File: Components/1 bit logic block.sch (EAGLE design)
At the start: 2 parts

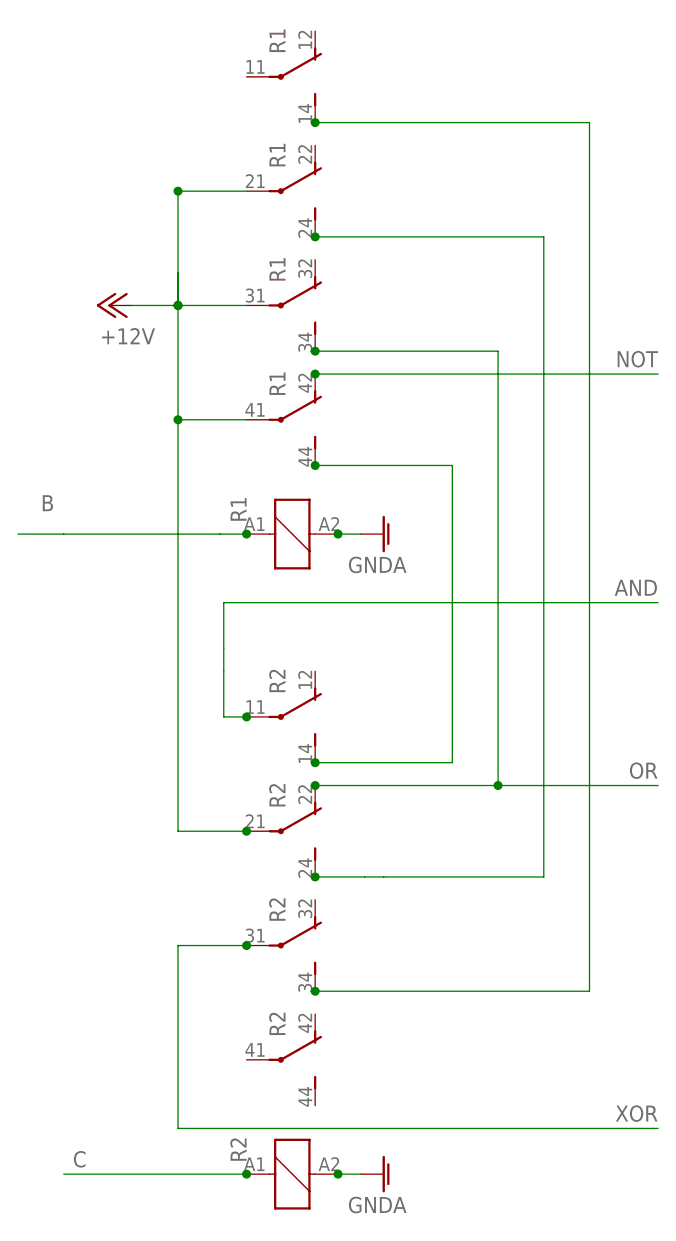
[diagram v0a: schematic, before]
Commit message: Fixed wiring for 1 bit logic block
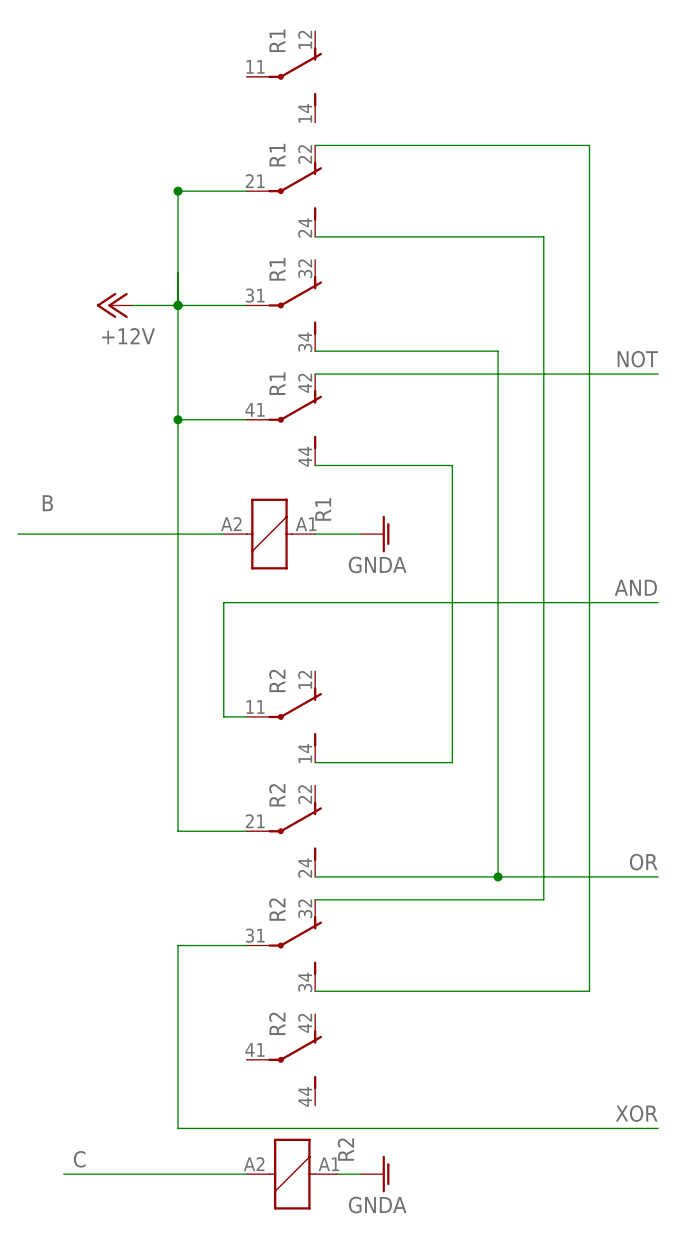
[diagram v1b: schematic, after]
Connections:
- net B: now also R11.2; no longer R11.1
- net C: now also R21.2; no longer R21.1
- net GNDA: now also R11.1, R21.1; no longer R11.2, R21.2
- net N$1: now also R24.O; no longer R23.S
- net N$3: now also R13.O; no longer R12.S
- net OR: now also R23.S; no longer R23.O
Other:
- moved on the sheet: R1
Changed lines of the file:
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@@
 <?xml version="1.0" encoding="utf-8"?>
 <!DOCTYPE eagle SYSTEM "eagle.dtd">
-<eagle version="8.1.0">
+<eagle version="8.2.1">
 <drawing>
 <settings>
@@
 <instance part="GND1" gate="1" x="96.52" y="91.44" rot="R90"/>
 <instance part="P+1" gate="1" x="66.04" y="116.84" rot="R90"/>
-<instance part="R1" gate="1" x="86.36" y="91.44" rot="R90"/>
+<instance part="R1" gate="1" x="83.82" y="91.44" rot="MR90"/>
 <instance part="R1" gate="2" x="83.82" y="142.24" rot="MR90"/>
 <instance part="R1" gate="3" x="83.82" y="129.54" rot="MR90"/>
 <instance part="R1" gate="4" x="83.82" y="116.84" rot="MR90"/>
 <instance part="R1" gate="5" x="83.82" y="104.14" rot="MR90"/>
-<instance part="R2" gate="1" x="86.36" y="20.32" rot="R90"/>
+<instance part="R2" gate="1" x="86.36" y="20.32" rot="MR90"/>
 <instance part="R2" gate="2" x="83.82" y="71.12" rot="MR90"/>
 <instance part="R2" gate="3" x="83.82" y="58.42" rot="MR90"/>
@@
 <net name="GNDA" class="0">
 <segment>
+<pinref part="GND2" gate="1" pin="GNDA"/>
+<wire x1="93.98" y1="20.32" x2="91.44" y2="20.32" width="0.1524" layer="91"/>
+<pinref part="R2" gate="1" pin="1"/>
+</segment>
+<segment>
+<pinref part="R1" gate="1" pin="1"/>
+<wire x1="88.9" y1="91.44" x2="93.98" y2="91.44" width="0.1524" layer="91"/>
+<pinref part="GND1" gate="1" pin="GNDA"/>
+</segment>
+</net>
+<net name="B" class="0">
+<segment>
+<label x="58.42" y="93.98" size="1.778" layer="95"/>
+<wire x1="55.88" y1="91.44" x2="78.74" y2="91.44" width="0.1524" layer="91"/>
 <pinref part="R1" gate="1" pin="2"/>
-<junction x="91.44" y="91.44"/>
-<pinref part="GND1" gate="1" pin="GNDA"/>
-<wire x1="91.44" y1="91.44" x2="93.98" y2="91.44" width="0.1524" layer="91"/>
-</segment>
-<segment>
-<pinref part="GND2" gate="1" pin="GNDA"/>
+</segment>
+</net>
+<net name="C" class="0">
+<segment>
+<label x="63.5" y="22.86" size="1.778" layer="95" rot="R180"/>
+<wire x1="60.96" y1="20.32" x2="81.28" y2="20.32" width="0.1524" layer="91"/>
 <pinref part="R2" gate="1" pin="2"/>
-<wire x1="93.98" y1="20.32" x2="91.44" y2="20.32" width="0.1524" layer="91"/>
-<junction x="91.44" y="20.32"/>
-</segment>
-</net>
-<net name="B" class="0">
-<segment>
-<wire x1="55.88" y1="91.44" x2="60.96" y2="91.44" width="0.1524" layer="91"/>
-<label x="58.42" y="93.98" size="1.778" layer="95"/>
-<pinref part="R1" gate="1" pin="1"/>
-<wire x1="60.96" y1="91.44" x2="78.327596875" y2="91.44" width="0.1524" layer="91"/>
-<wire x1="81.28" y1="91.44" x2="78.327596875" y2="91.44" width="0.1524" layer="91"/>
-<junction x="81.28" y="91.44"/>
-</segment>
-</net>
-<net name="C" class="0">
-<segment>
-<label x="63.5" y="22.86" size="1.778" layer="95" rot="R180"/>
-<pinref part="R2" gate="1" pin="1"/>
-<wire x1="60.96" y1="20.32" x2="81.28" y2="20.32" width="0.1524" layer="91"/>
-<junction x="81.28" y="20.32"/>
 </segment>
 </net>
@@
 <junction x="73.66" y="104.14"/>
 <wire x1="73.66" y1="116.84" x2="73.66" y2="120.4952875" width="0.1524" layer="91"/>
-<pinref part="R1" gate="5" pin="P"/>
 <wire x1="73.66" y1="104.14" x2="81.28" y2="104.14" width="0.1524" layer="91"/>
 <junction x="73.66" y="116.84"/>
-<pinref part="R1" gate="4" pin="P"/>
 <wire x1="73.66" y1="116.84" x2="81.28" y2="116.84" width="0.1524" layer="91"/>
 <junction x="73.66" y="129.54"/>
+<wire x1="73.66" y1="129.54" x2="81.28" y2="129.54" width="0.1524" layer="91"/>
+<wire x1="81.28" y1="58.42" x2="73.66" y2="58.42" width="0.1524" layer="91"/>
+<pinref part="R1" gate="5" pin="P"/>
+<pinref part="R1" gate="4" pin="P"/>
 <pinref part="R1" gate="3" pin="P"/>
-<wire x1="73.66" y1="129.54" x2="81.28" y2="129.54" width="0.1524" layer="91"/>
 <pinref part="R2" gate="3" pin="P"/>
-<wire x1="81.28" y1="58.42" x2="73.66" y2="58.42" width="0.1524" layer="91"/>
-<junction x="81.28" y="58.42"/>
 </segment>
 </net>
@@
 <wire x1="73.66" y1="25.4" x2="127" y2="25.4" width="0.1524" layer="91"/>
 <label x="127" y="27.94" size="1.778" layer="95" rot="R180"/>
+<wire x1="81.28" y1="45.72" x2="73.66" y2="45.72" width="0.1524" layer="91"/>
 <pinref part="R2" gate="4" pin="P"/>
-<wire x1="81.28" y1="45.72" x2="73.66" y2="45.72" width="0.1524" layer="91"/>
-<junction x="81.28" y="45.72"/>
 </segment>
 </net>
 <net name="AND" class="0">
 <segment>
-<wire x1="78.74" y1="76.2" x2="78.74" y2="78.74" width="0.1524" layer="91"/>
-<wire x1="78.74" y1="78.74" x2="78.74" y2="83.82" width="0.1524" layer="91"/>
 <wire x1="78.74" y1="83.82" x2="127" y2="83.82" width="0.1524" layer="91"/>
 <label x="127" y="86.36" size="1.778" layer="95" rot="R180"/>
+<wire x1="81.28" y1="71.12" x2="78.74" y2="71.12" width="0.1524" layer="91"/>
+<wire x1="78.74" y1="71.12" x2="78.74" y2="83.82" width="0.1524" layer="91"/>
 <pinref part="R2" gate="2" pin="P"/>
-<junction x="81.28" y="71.12"/>
-<wire x1="81.28" y1="71.12" x2="78.74" y2="71.12" width="0.1524" layer="91"/>
-<wire x1="78.74" y1="71.12" x2="78.74" y2="76.2" width="0.1524" layer="91"/>
 </segment>
 </net>
@@
 <wire x1="88.9" y1="109.22" x2="127" y2="109.22" width="0.1524" layer="91"/>
 <pinref part="R1" gate="5" pin="O"/>
-<junction x="88.9" y="109.22"/>
 </segment>
 </net>
 <net name="OR" class="0">
 <segment>
-<label x="127" y="66.04" size="1.778" layer="95" rot="R180"/>
-<wire x1="109.22" y1="63.5" x2="127" y2="63.5" width="0.1524" layer="91"/>
-<wire x1="109.22" y1="111.76" x2="109.22" y2="63.5" width="0.1524" layer="91"/>
+<label x="127" y="55.88" size="1.778" layer="95" rot="R180"/>
+<wire x1="109.22" y1="53.34" x2="127" y2="53.34" width="0.1524" layer="91"/>
+<wire x1="109.22" y1="111.76" x2="109.22" y2="53.34" width="0.1524" layer="91"/>
+<wire x1="88.9" y1="111.76" x2="109.22" y2="111.76" width="0.1524" layer="91"/>
 <pinref part="R1" gate="4" pin="S"/>
-<junction x="88.9" y="111.76"/>
-<wire x1="88.9" y1="111.76" x2="109.22" y2="111.76" width="0.1524" layer="91"/>
-<pinref part="R2" gate="3" pin="O"/>
-<junction x="88.9" y="63.5"/>
-<wire x1="88.9" y1="63.5" x2="109.22" y2="63.5" width="0.1524" layer="91"/>
-<junction x="109.22" y="63.5"/>
+<pinref part="R2" gate="3" pin="S"/>
+<wire x1="88.9" y1="53.34" x2="109.22" y2="53.34" width="0.1524" layer="91"/>
+<junction x="109.22" y="53.34"/>
 </segment>
 </net>
 <net name="N$1" class="0">
 <segment>
-<pinref part="R2" gate="3" pin="S"/>
-<junction x="88.9" y="53.34"/>
+<wire x1="114.3" y1="50.8" x2="114.3" y2="124.46" width="0.1524" layer="91"/>
+<wire x1="88.9" y1="124.46" x2="114.3" y2="124.46" width="0.1524" layer="91"/>
 <pinref part="R1" gate="3" pin="S"/>
-<junction x="88.9" y="124.46"/>
-<wire x1="94.392403125" y1="53.34" x2="96.52" y2="53.34" width="0.1524" layer="91"/>
-<wire x1="96.52" y1="53.34" x2="114.3" y2="53.34" width="0.1524" layer="91"/>
-<wire x1="114.3" y1="53.34" x2="114.3" y2="124.46" width="0.1524" layer="91"/>
-<wire x1="88.9" y1="124.46" x2="114.3" y2="124.46" width="0.1524" layer="91"/>
-<wire x1="88.9" y1="53.34" x2="94.392403125" y2="53.34" width="0.1524" layer="91"/>
+<pinref part="R2" gate="4" pin="O"/>
+<wire x1="88.9" y1="50.8" x2="114.3" y2="50.8" width="0.1524" layer="91"/>
 </segment>
 </net>
 <net name="N$3" class="0">
 <segment>
+<wire x1="119.38" y1="134.62" x2="119.38" y2="40.64" width="0.1524" layer="91"/>
+<wire x1="88.9" y1="40.64" x2="119.38" y2="40.64" width="0.1524" layer="91"/>
 <pinref part="R2" gate="4" pin="S"/>
-<junction x="88.9" y="40.64"/>
-<pinref part="R1" gate="2" pin="S"/>
-<junction x="88.9" y="137.16"/>
-<wire x1="119.38" y1="137.16" x2="119.38" y2="45.72" width="0.1524" layer="91"/>
-<wire x1="119.38" y1="45.72" x2="119.38" y2="41.7552875" width="0.1524" layer="91"/>
-<wire x1="88.9" y1="137.16" x2="119.38" y2="137.16" width="0.1524" layer="91"/>
-<wire x1="88.9" y1="40.64" x2="119.38" y2="40.64" width="0.1524" layer="91"/>
-<wire x1="119.38" y1="40.64" x2="119.38" y2="41.7552875" width="0.1524" layer="91"/>
+<pinref part="R1" gate="3" pin="O"/>
+<wire x1="88.9" y1="134.62" x2="119.38" y2="134.62" width="0.1524" layer="91"/>
 </segment>
 </net>
 <net name="N$2" class="0">
 <segment>
+<wire x1="88.9" y1="99.06" x2="104.14" y2="99.06" width="0.1524" layer="91"/>
+<wire x1="104.14" y1="99.06" x2="104.14" y2="66.04" width="0.1524" layer="91"/>
+<wire x1="88.9" y1="66.04" x2="104.14" y2="66.04" width="0.1524" layer="91"/>
 <pinref part="R1" gate="5" pin="S"/>
-<junction x="88.9" y="99.06"/>
-<wire x1="89.312403125" y1="99.06" x2="93.98" y2="99.06" width="0.1524" layer="91"/>
-<wire x1="93.98" y1="99.06" x2="104.14" y2="99.06" width="0.1524" layer="91"/>
-<wire x1="104.14" y1="99.06" x2="104.14" y2="66.04" width="0.1524" layer="91"/>
 <pinref part="R2" gate="2" pin="S"/>
-<wire x1="88.9" y1="66.04" x2="104.14" y2="66.04" width="0.1524" layer="91"/>
-<wire x1="88.9" y1="99.06" x2="89.312403125" y2="99.06" width="0.1524" layer="91"/>
-<junction x="88.9" y="66.04"/>
-</segment>
-</net>
+</segment>
+</net>
